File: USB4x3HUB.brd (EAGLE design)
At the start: 90 x 90 mm, 100 parts, among them IC1 TUSB2036, IC10 SN74LVC1G139DCUR, IC2 FSUSB74MPX, IC6 3.3V, IC7 5V, IC8 5V, IC9 5V, Q1 48M/3225, SW1 RD, SW2 BL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

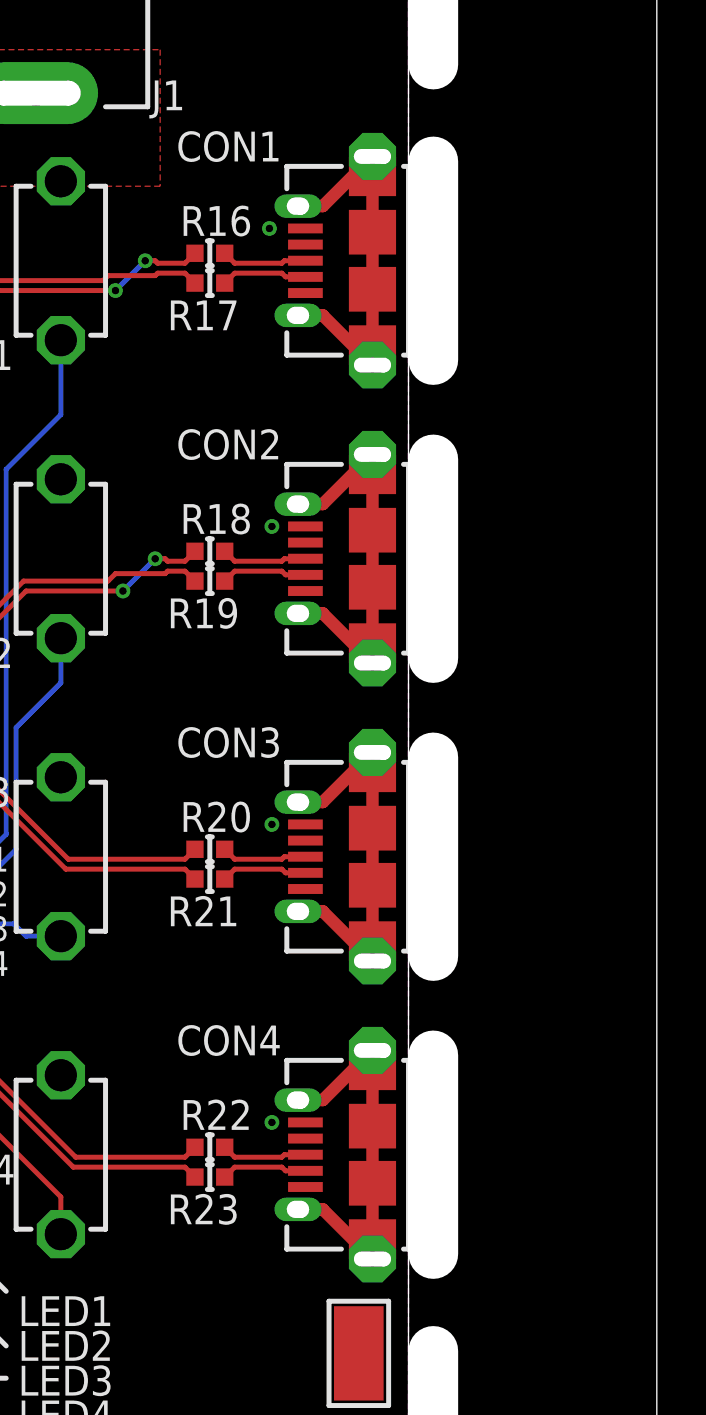
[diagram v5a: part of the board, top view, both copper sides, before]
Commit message: library update: CON1-4 milling and IC10 attribute
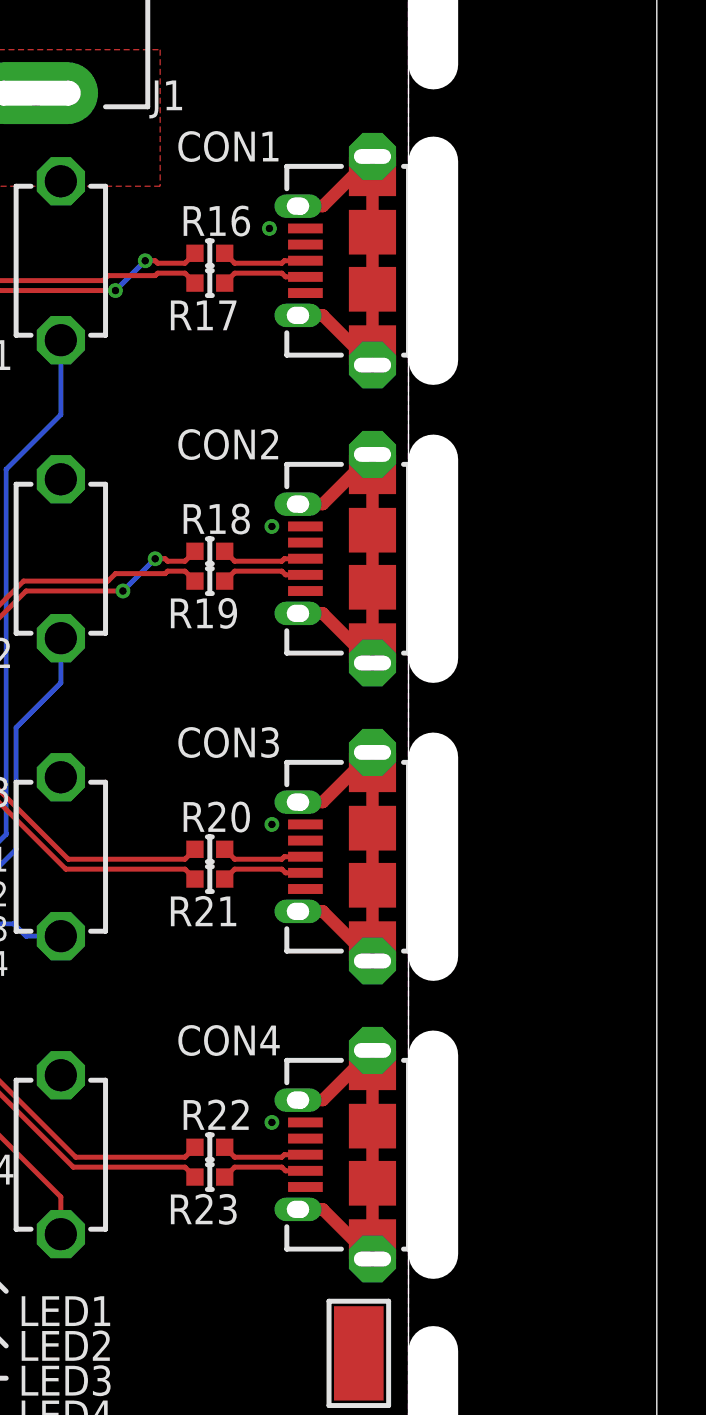
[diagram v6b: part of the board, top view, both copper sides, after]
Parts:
- GIT1: value 215f3cd -> 942afa9
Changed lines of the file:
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@@
 <attribute name="NAME" x="61.9" y="29.2" size="1" layer="25" font="vector" ratio="20" align="center"/>
 <attribute name="VALUE" x="61.7" y="26.7" size="1" layer="27" font="vector" ratio="20" rot="R90"/>
-<attribute name="DIGIKEY" value="296-18203-1-ND" x="58.4" y="29.2" size="1.778" layer="27" display="off"/>
+<attribute name="DIGIKEY" value="296-18235-1-ND" x="58.4" y="29.2" size="1.778" layer="27" display="off"/>
 </element>
 <element name="C20" library="mylib" package="C0402" value="" x="58.2" y="32.5" smashed="yes">
@@
 <attribute name="VALUE" x="45.281" y="37.346" size="0.0254" layer="27" rot="R90"/>
 </element>
-<element name="GIT1" library="git-revision" package="GIT-REVISION" value="215f3cd" x="10" y="10"/>
+<element name="GIT1" library="git-revision" package="GIT-REVISION" value="942afa9" x="10" y="10"/>
 <element name="TP1" library="mylib" package="TP_4020" value="" x="78" y="19" rot="R90">
 <attribute name="DIGIKEY" value="36-5019CT-ND" x="78" y="19" size="1.778" layer="27" rot="R90" display="off"/>
@@
 <contactref element="TP2" pad="TP"/>
 <contactref element="TP2" pad="TP"/>
+<via x="57.7" y="35.4" extent="1-16" drill="0.3"/>
 <contactref element="CON1" pad="5"/>
 <contactref element="CON2" pad="5"/>
@@
 <contactref element="CON6" pad="4"/>
 <contactref element="CON7" pad="4"/>
-<via x="57.7" y="35.4" extent="1-16" drill="0.3"/>
 </signal>
 <signal name="AVSS">

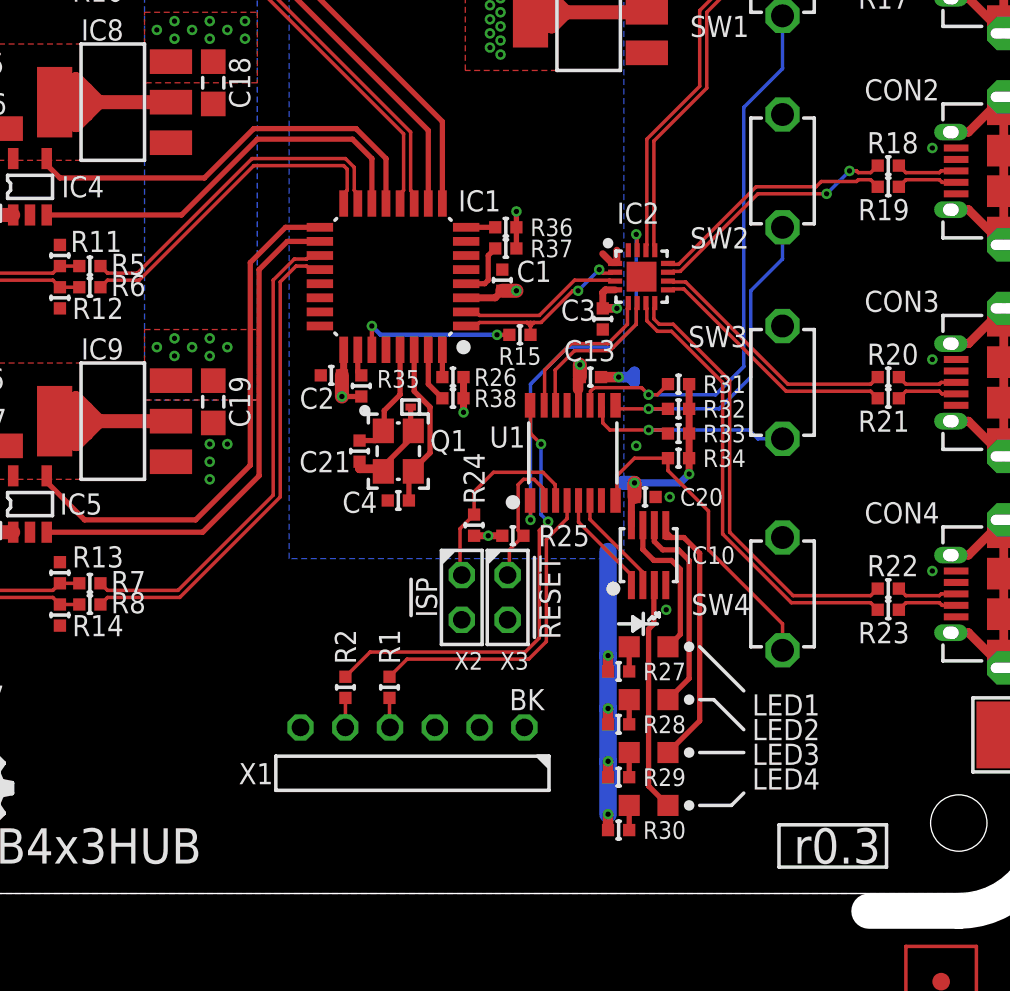
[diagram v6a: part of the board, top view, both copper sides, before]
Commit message: replace Q1 to use Oscillator add R39~45; add TP3; remove C21
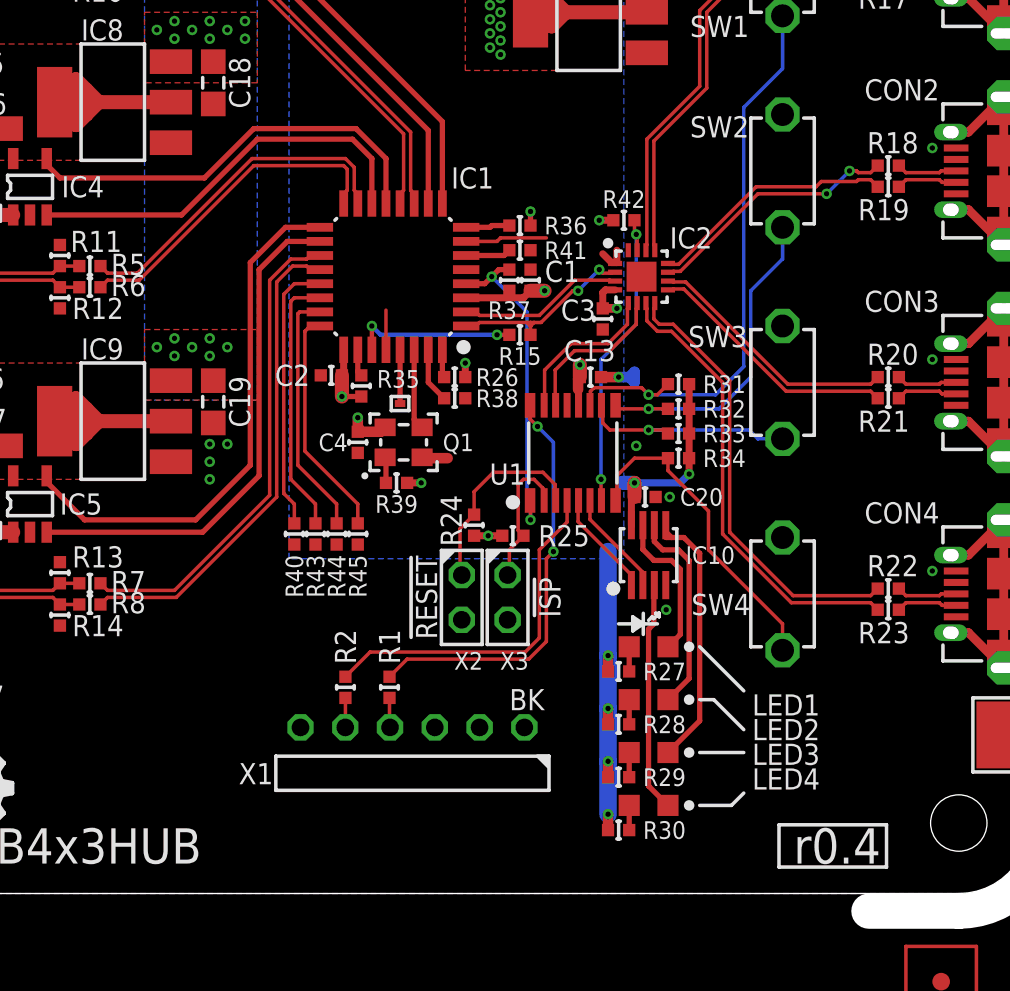
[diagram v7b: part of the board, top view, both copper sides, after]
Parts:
- removed C21: (no value), mylib:C0402
- added R39, R40, R41, R42, R43, R44, R45: (no value), mylib:C0402
- ICON2: value r0.3 -> r0.4
- Q1: value 48M/3225 -> CLOCK_OSC_4; device mylib:CLOCK_3225 -> mylib:CLOCK_2520
- moved C4 4.02 mm to (41.9, 35.6), turned to 270 degrees
- moved R37 1.81 mm to (50.5, 44.8), turned to 90 degrees
- moved C1 1.60 mm to (51.7, 44.8)
- moved R36 0.81 mm to (51.1, 47.9)
- moved TP3 0.63 mm to (44.3, 37.8)
- moved Q1 0.58 mm to (44.5, 35.6), turned to 0 degrees
- moved R26 0.10 mm to (47.4, 39.3)
- moved R38 0.10 mm to (47.4, 38.1)
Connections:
- new net N$30: IC1.6, R41.1
- new net N$64: IC1.21, R40.2
- new net N$65: IC1.24, R45.2
- new net N$66: IC1.23, R44.2
- new net N$67: IC1.22, R43.2
- new net N$68: Q1.1, R39.2
- net !OE!: now also R42.2, U1.7; no longer U1.1
- net 3.3V: now also C4.1, Q1.4, R39.1, R42.1; no longer R38.1
- net GND: now also R38.1, R40.1, R41.2, R43.1, R44.1, R45.1; no longer C21.2, IC1.21, IC1.22, IC1.23, IC1.24, IC1.6, Q1.4, TP3.TP
- net N$15: no longer C4.1
- net N$59: now also TP3.TP; no longer C21.1, Q1.1
- net N$62: now also U1.1
- net TGT_RX: now also U1.16; no longer U1.4
- net TGT_TX: now also U1.4; no longer U1.16
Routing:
- net N$64: track 0.00 -> 15.5 mm
- net N$62: track 3.30 -> 18.6 mm, vias 0 -> 2
- net N$67: track 0.00 -> 14.9 mm
- net N$66: track 0.00 -> 14.1 mm
- net N$65: track 0.00 -> 13.1 mm
- net TGT_RX: track 18.2 -> 23.8 mm, vias 0 -> 2
- net TGT_TX: track 25.8 -> 20.4 mm, vias 2 -> 0
- net N$15: track 9.46 -> 4.59 mm
- net !OE!: track 22.2 -> 17.7 mm
- net N$59: track 6.70 -> 3.05 mm
- net 3.3V: track 57.9 -> 61.4 mm, vias 26 -> 29
- net N$30: track 0.00 -> 2.57 mm
- net GND: track 11.3 -> 13.8 mm
- net N$68: track 0.00 -> 1.47 mm
- net N$61: track 1.65 -> 2.49 mm

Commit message: library update; add DIGIKEY attributes
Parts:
- Q1: value CLOCK_OSC_4 -> OSC4_6.0M
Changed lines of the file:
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@@
 <attribute name="VALUE" x="57" y="48.2" size="1" layer="27" font="vector" align="center"/>
 </element>
-<element name="Q1" library="mylib" package="CLOCK_2520" value="CLOCK_OSC_4" x="44.5" y="35.6" smashed="yes">
+<element name="Q1" library="mylib" package="CLOCK_2520" value="OSC4_6.0M" x="44.5" y="35.6" smashed="yes">
 <attribute name="NAME" x="47.6" y="35.6" size="1" layer="25" font="vector" ratio="20" align="center"/>
+<attribute name="DIGIKEY" value="CTX974CT-ND" x="44.5" y="35.6" size="1.778" layer="27" display="off"/>
 </element>
 <element name="TP3" library="mylib" package="TP06RECT" value="" x="44.3" y="37.8" rot="R90">
